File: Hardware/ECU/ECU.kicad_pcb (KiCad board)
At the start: 2 copper layers, 148 x 111.5 mm, 162 parts, among them IC1 MAX9926UAEE_V+, IC2 ZXMS6006DT8, IC3 ZXMS6006DT8, IC4 ZXMS6006DT8, J1 Conn_01x04, Q1 Q_DUAL_NMOS_S1G1D2S2G2D1, Q2 Q_DUAL_NMOS_S1G1D2S2G2D1, Q3 Q_PNP_BCEC, Q4 IRFB4110PBF, Q5 IRFB4110PBF, Q6 IRFB4110PBF, Q7 IRFB4110PBF, SW1 SW_DPDT_x2, SW2 SW_DPDT_x2, SW3 SW_DIP_x02, SW4 SW_DPDT_x2, U1 Teensy4.1, U12 LMV324LIDT, U13 SP720, U14 LMV324LIDT, U15 MC33814, U16 TC4424A, U17 W25Q32JVSS, U3 74AHC1G32, U4 ADXL343, U5 TC4424A, U7 MC33810, U9 TC4424A

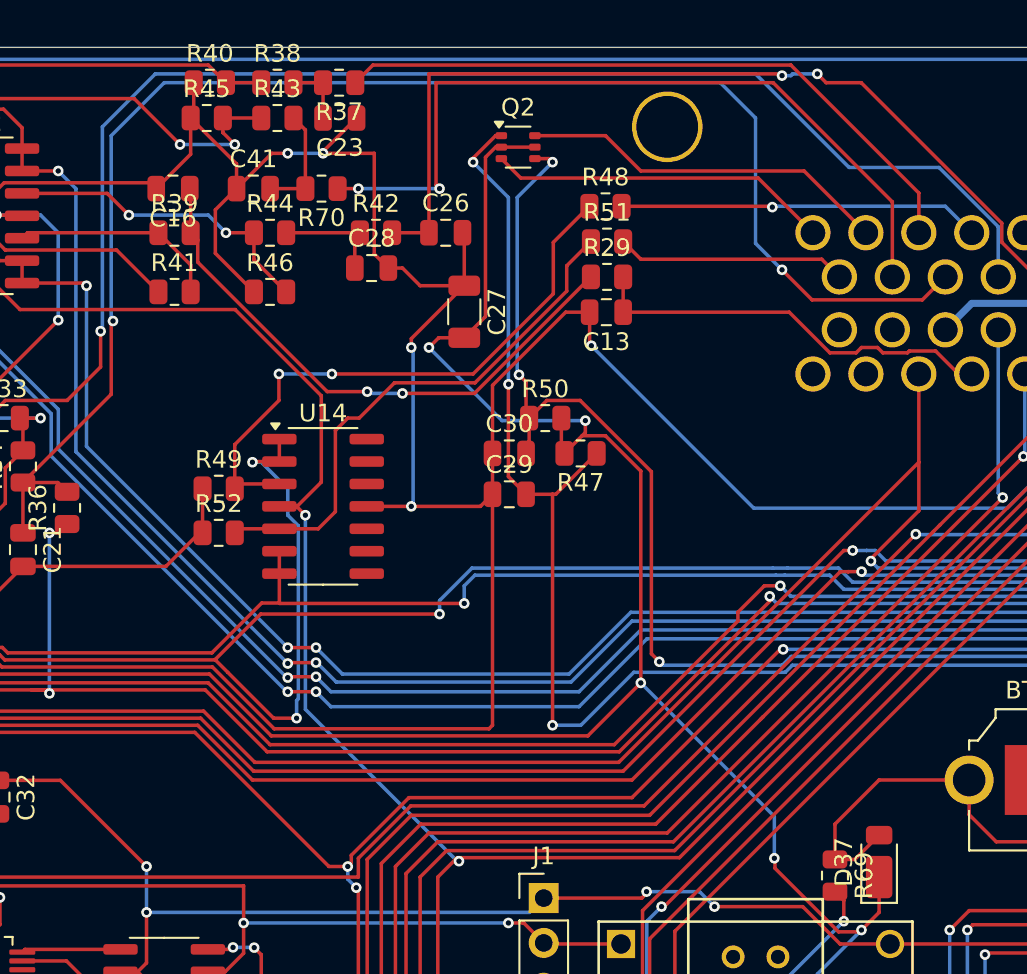
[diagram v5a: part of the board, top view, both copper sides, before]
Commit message: modified:   Hardware/ECU/Conntectors.kicad_sch deleted:    Hardware/ECU/ECU-backups/ECU-2025-05-14_000421.zip deleted:    Hardware/ECU/ECU-backups/ECU-2025-05-14_001426.zip deleted:    Hardware/ECU/ECU-backups/ECU-2025-05-14_002531.zip deleted:    Hardware/ECU/ECU-backups/ECU-2025-05-14_003555.zip deleted:    Hardware/ECU/ECU-backups/ECU-2025-05-14_004055.zip modified:   Hardware/ECU/ECU.kicad_pcb modified:   Hardware/ECU/ECU.kicad_prl modified:   Hardware/ECU/ECU.kicad_pro modified:   Hardware/ECU/ECU.kicad_sch 	modified:   Hardware/ECU/Inputs.kicad_sch 	modified:   Hardware/ECU/Inputs2.kicad_sch 	modified:   Hardware/ECU/Schematics.pdf 	modified:   Hardware/ECU/docs/Pinout.ods 	Hardware/ECU/ECU-backups/ECU-2025-05-19_135220.zip 	Hardware/ECU/ECU-backups/ECU-2025-05-19_140656.zip 	Hardware/ECU/ECU-backups/ECU-2025-05-19_142320.zip 	Hardware/ECU/ECU-backups/ECU-2025-05-19_145225.zip 	Hardware/ECU/ECU-backups/ECU-2025-05-19_160311.zip 	Hardware/ECU/ECU.kicad_pcb.zip 	Hardware/ECU/docs/GPS.JPG 	docs/Kabelplan.pdn
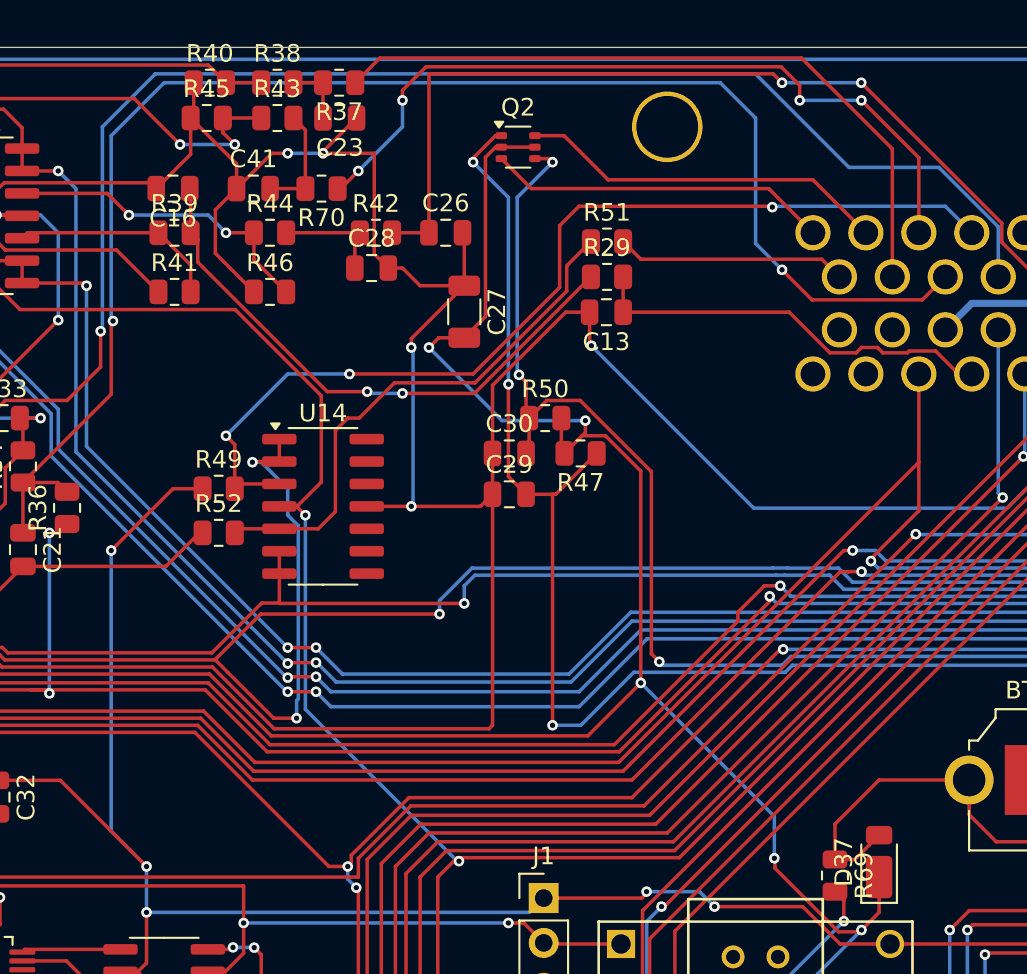
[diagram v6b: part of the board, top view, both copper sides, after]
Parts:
- removed R48: 180k, Resistor_SMD:R_0805_2012Metric
- R49: value 348k -> 1k
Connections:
- net /Conntectors/Fuel pump FB renamed /Conntectors/FI FB
- J5 pad 11: /Conntectors/NC -> unconnected-(J5-Pad11)
- J5 pad 12: /Conntectors/NC -> unconnected-(J5-Pad12)
- J5 pad 13: /Conntectors/NC -> unconnected-(J5-Pad13)
- J5 pad 33: /Conntectors/NC -> unconnected-(J5-Pad33)
- J5 pad 34: /Conntectors/NC -> unconnected-(J5-Pad34)
- J5 pad 40: /Conntectors/NC -> unconnected-(J5-Pad40)
- J5 pad 41: /Conntectors/NC -> unconnected-(J5-Pad41)
- J5 pad 46: /Conntectors/NC -> unconnected-(J5-Pad46)
- J5 pad 47: /Conntectors/NC -> unconnected-(J5-Pad47)
- J5 pad 52: Static_Air -> Baro_Sensor
- J5 pad 58: Baro_Sensor -> Map_Sensor
- R49 pad 1: GND -> +5V
- R49 pad 2: Net-(U14A-+) -> Gear_Position
- R70 pad 1: Static_Air -> Map_Sensor
- U14 pad 3: Net-(U14A-+) -> Gear_Position
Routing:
- net Static_Air: track 44.8 -> 0.00 mm, vias 2 -> 0
- net Map_Sensor: track 0.00 -> 43.9 mm, vias 0 -> 4
- net Gear_Position: track 20.5 -> 56.2 mm, vias 1 -> 3
- net Net-(U14A-+): track 33.4 -> 0.00 mm, vias 2 -> 0
- net +5V: track 235.5 -> 260.8 mm, vias 16 -> 17
- net Baro_Sensor: track 37.6 -> 40.4 mm
- net GND: track 1211.3 -> 1208.8 mm

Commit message: modified:   Hardware/ECU/Drivers.kicad_sch 	deleted:    Hardware/ECU/ECU-backups/ECU-2025-05-15_143348.zip 	deleted:    Hardware/ECU/ECU-backups/ECU-2025-05-15_144355.zip 	deleted:    Hardware/ECU/ECU-backups/ECU-2025-05-15_152109.zip 	deleted:    Hardware/ECU/ECU-backups/ECU-2025-05-15_161628.zip 	deleted:    Hardware/ECU/ECU-backups/ECU-2025-05-15_162311.zip 	deleted:    Hardware/ECU/ECU-backups/ECU-2025-05-16_191516.zip 	deleted:    Hardware/ECU/ECU-backups/ECU-2025-05-16_192518.zip 	deleted:    Hardware/ECU/ECU-backups/ECU-2025-05-16_193610.zip 	new file:   Hardware/ECU/ECU-backups/ECU-2025-05-20_084251.zip 	new file:   Hardware/ECU/ECU-backups/ECU-2025-05-20_085713.zip 	new file:   Hardware/ECU/ECU-backups/ECU-2025-05-20_090304.zip 	new file:   Hardware/ECU/ECU-backups/ECU-2025-05-20_142748.zip 	new file:   Hardware/ECU/ECU-backups/ECU-2025-05-20_150003.zip 	new file:   Hardware/ECU/ECU-backups/ECU-2025-05-27_131057.zip 	new file:   Hardware/ECU/ECU-backups/ECU-2025-05-27_141528.zip 	new file:   Hardware/ECU/ECU-backups/ECU-2025-05-27_154948.zip 	new file:   Hardware/ECU/ECU-backups/ECU-2025-05-27_155558.zip 	new file:   Hardware/ECU/ECU.csv 	modified:   Hardware/ECU/ECU.kicad_pcb 	modified:   Hardware/ECU/ECU.kicad_pcb.zip 	new file:   Hardware/ECU/ECU.xml 	modified:   Hardware/ECU/Power-Regulator.kicad_sch 	modified:   Hardware/ECU/docs/Pinout.ods 	modified:   Hardware/ECU/fp-info-cache 	modified:   Hardware/ECU/fp-lib-table 	new file:   Hardware/ECU/lib/CRCW060349K9FKEAC.step 	new file:   Hardware/ECU/lib/CRCW060349K9FKEAC.wrl 	new file:   Hardware/ECU/lib/GRM21BC81A226ME44L.step 	new file:   Hardware/ECU/lib/GRM21BC81A226ME44L.wrl 	new file:   Hardware/ECU/lib/SamacSys_Parts.3dshapes/NE555DR.stp 	new file:   Hardware/ECU/lib/SamacSys_Parts.dcm 	new file:   Hardware/ECU/lib/SamacSys_Parts.kicad_sym 	new file:   Hardware/ECU/lib/SamacSys_Parts.lib 	new file:   Hardware/ECU/lib/SamacSys_Parts.mod 	new file:   Hardware/ECU/lib/SamacSys_Parts.pretty/NE555DR.kica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
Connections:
- net MC33810_2-CS renamed MCU-D9
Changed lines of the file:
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@@
 			(psa4output no)
 			(plot_black_and_white yes)
+			(plotinvisibletext no)
 			(sketchpadsonfab no)
 			(plotpadnumbers no)
@@
 	(net 155 "unconnected-(U1-GND-Pad64)")
 	(net 156 "ADC-Clamp-14")
-	(net 157 "MC33810_2-CS")
+	(net 157 "MCU-D9")
 	(net 158 "MOSI")
 	(net 159 "Net-(U4-SDA{slash}SDI{slash}SDIO)")
@@
 			(layers "*.Cu" "*.Mask")
 			(remove_unused_layers no)
-			(net 157 "MC33810_2-CS")
+			(net 157 "MCU-D9")
 			(pinfunction "9_OUT1C")
 			(pintype "bidirectional")
